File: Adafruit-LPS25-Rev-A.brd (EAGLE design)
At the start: 25.4 x 17.8 mm, 24 parts, among them Q2 BSS138, U2 AP2112K-3.3

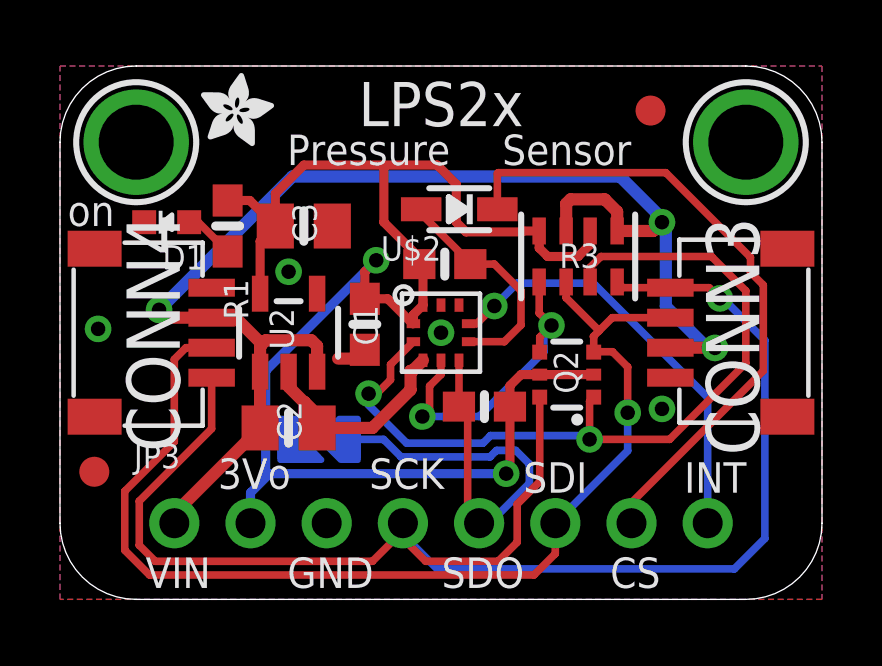
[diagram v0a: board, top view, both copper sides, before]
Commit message: adding LPS22
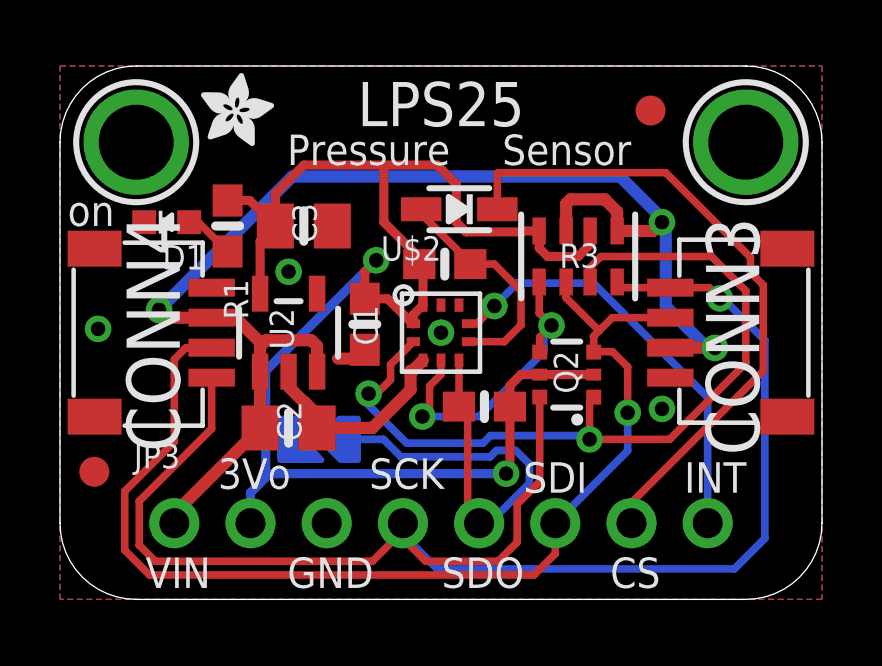
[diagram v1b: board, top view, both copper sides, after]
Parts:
- U$2: value LPS2XHLGA -> LPS2X_LPS25
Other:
- board text added: "Default I2C Addr 0x5D"
- board text added: "LPS25"
- board text added: "ST LPS25"
- board text removed: "I2C Addr 0x5D"
- board text removed: "LPS2x"
- board text removed: "ST LPS2x"
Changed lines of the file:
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@@
 <setting verticaltext="up"/>
 </settings>
-<grid distance="5" unitdist="mil" unit="mil" style="lines" multiple="1" display="yes" altdistance="1" altunitdist="mil" altunit="mil"/>
+<grid distance="2.5" unitdist="mil" unit="mil" style="lines" multiple="1" display="yes" altdistance="1" altunitdist="mil" altunit="mil"/>
 <layers>
-<layer number="1" name="Top" color="4" fill="1" visible="no" active="yes"/>
+<layer number="1" name="Top" color="4" fill="1" visible="yes" active="yes"/>
 <layer number="2" name="Route2" color="1" fill="3" visible="no" active="no"/>
 <layer number="3" name="Route3" color="4" fill="3" visible="no" active="no"/>
@@
 <layer number="14" name="Route14" color="1" fill="6" visible="no" active="no"/>
 <layer number="15" name="Route15" color="4" fill="6" visible="no" active="no"/>
-<layer number="16" name="Bottom" color="9" fill="1" visible="no" active="yes"/>
+<layer number="16" name="Bottom" color="9" fill="1" visible="yes" active="yes"/>
 <layer number="17" name="Pads" color="2" fill="1" visible="yes" active="yes"/>
-<layer number="18" name="Vias" color="2" fill="1" visible="no" active="yes"/>
+<layer number="18" name="Vias" color="2" fill="1" visible="yes" active="yes"/>
 <layer number="19" name="Unrouted" color="11" fill="1" visible="yes" active="yes"/>
 <layer number="20" name="Dimension" color="15" fill="1" visible="yes" active="yes"/>
-<layer number="21" name="tPlace" color="14" fill="1" visible="no" active="yes"/>
-<layer number="22" name="bPlace" color="13" fill="1" visible="no" active="yes"/>
-<layer number="23" name="tOrigins" color="14" fill="1" visible="no" active="yes"/>
-<layer number="24" name="bOrigins" color="13" fill="1" visible="no" active="yes"/>
+<layer number="21" name="tPlace" color="14" fill="1" visible="yes" active="yes"/>
+<layer number="22" name="bPlace" color="13" fill="1" visible="yes" active="yes"/>
+<layer number="23" name="tOrigins" color="14" fill="1" visible="yes" active="yes"/>
+<layer number="24" name="bOrigins" color="13" fill="1" visible="yes" active="yes"/>
 <layer number="25" name="tNames" color="7" fill="1" visible="no" active="yes"/>
 <layer number="26" name="bNames" color="7" fill="1" visible="no" active="yes"/>
-<layer number="27" name="tValues" color="11" fill="1" visible="yes" active="yes"/>
+<layer number="27" name="tValues" color="11" fill="1" visible="no" active="yes"/>
 <layer number="28" name="bValues" color="7" fill="1" visible="no" active="yes"/>
 <layer number="29" name="tStop" color="7" fill="3" visible="no" active="yes"/>
@@
 <text x="16.51" y="4.064" size="1.016" layer="21" font="vector" ratio="14" align="center">SDI</text>
 <text x="21.844" y="4.064" size="1.016" layer="21" font="vector" ratio="14" align="center">INT</text>
-<text x="12.7" y="16.51" size="1.4732" layer="21" font="vector" ratio="15" align="center">LPS2x</text>
+<text x="12.7" y="16.51" size="1.4732" layer="21" font="vector" ratio="15" align="center">LPS25</text>
 <text x="10.287" y="14.986" size="1.016" layer="21" font="vector" ratio="15" align="center">Pressure</text>
 <dimension x1="12.7" y1="2.54" x2="12.7" y2="15.24" x3="29.337" y3="8.89" textsize="1.778" layer="47" dtype="vertical" unit="inch"/>
@@
 <dimension x1="13.208" y1="0" x2="12.319" y2="17.78" x3="32.131" y3="8.89" textsize="1.778" layer="47" dtype="vertical" unit="inch"/>
 <text x="0.254" y="12.446" size="1.016" layer="21" font="vector" ratio="12">on</text>
-<text x="12.7" y="16.51" size="1.524" layer="22" font="vector" ratio="15" rot="MR0" align="center">ST LPS2x</text>
+<text x="12.7" y="16.51" size="1.524" layer="22" font="vector" ratio="15" rot="MR0" align="center">ST LPS25</text>
 <text x="12.7" y="14.732" size="1.2192" layer="22" font="vector" ratio="15" rot="MR0" align="center">Pressure Sensor</text>
-<text x="12.446" y="9.398" size="1.016" layer="22" font="vector" ratio="12" rot="MR0" align="center">VLogic/Vcc: 3-5VDC</text>
+<text x="12.446" y="0.762" size="1.016" layer="22" font="vector" ratio="12" rot="MR0" align="center">VLogic/Vcc: 3-5VDC</text>
 <text x="16.891" y="14.986" size="1.016" layer="21" font="vector" ratio="15" align="center">Sensor</text>
 <text x="12.7" y="12.7" size="1.2192" layer="22" font="vector" ratio="15" rot="MR0" align="center">260-1260 hPa</text>
@@
 <text x="14.097" y="0.889" size="1.016" layer="21" font="vector" ratio="14" align="center">SDO</text>
 <text x="8.382" y="7.112" size="1.016" layer="22" font="vector" ratio="15" rot="MR180" align="center">Addr</text>
-<text x="12.7" y="10.922" size="1.016" layer="22" font="vector" ratio="12" rot="MR0" align="center">I2C Addr 0x5D</text>
+<text x="12.7" y="10.922" size="1.016" layer="22" font="vector" ratio="12" rot="MR0" align="center">Default I2C Addr 0x5D</text>
 </plain>
 <attributes>
@@
 <attribute name="VALUE" x="11.557" y="11.049" size="1.016" layer="27" font="vector" ratio="10" rot="R90"/>
 </element>
-<element name="U$2" library="adafruit_sensor" package="HLGA-10L" value="LPS2XHLGA" x="12.7" y="8.89" smashed="yes">
+<element name="U$2" library="adafruit_sensor" package="HLGA-10L" value="LPS2X_LPS25" x="12.7" y="8.89" smashed="yes">
 <attribute name="NAME" x="10.69786875" y="11.29255" size="0.8128" layer="25" ratio="18"/>
 <attribute name="VALUE" x="7.879" y="18.763" size="1.016" layer="27" ratio="10"/>
